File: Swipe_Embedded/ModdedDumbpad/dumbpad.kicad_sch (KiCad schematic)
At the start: 17 parts, among them U1 ESP32-DevKitC

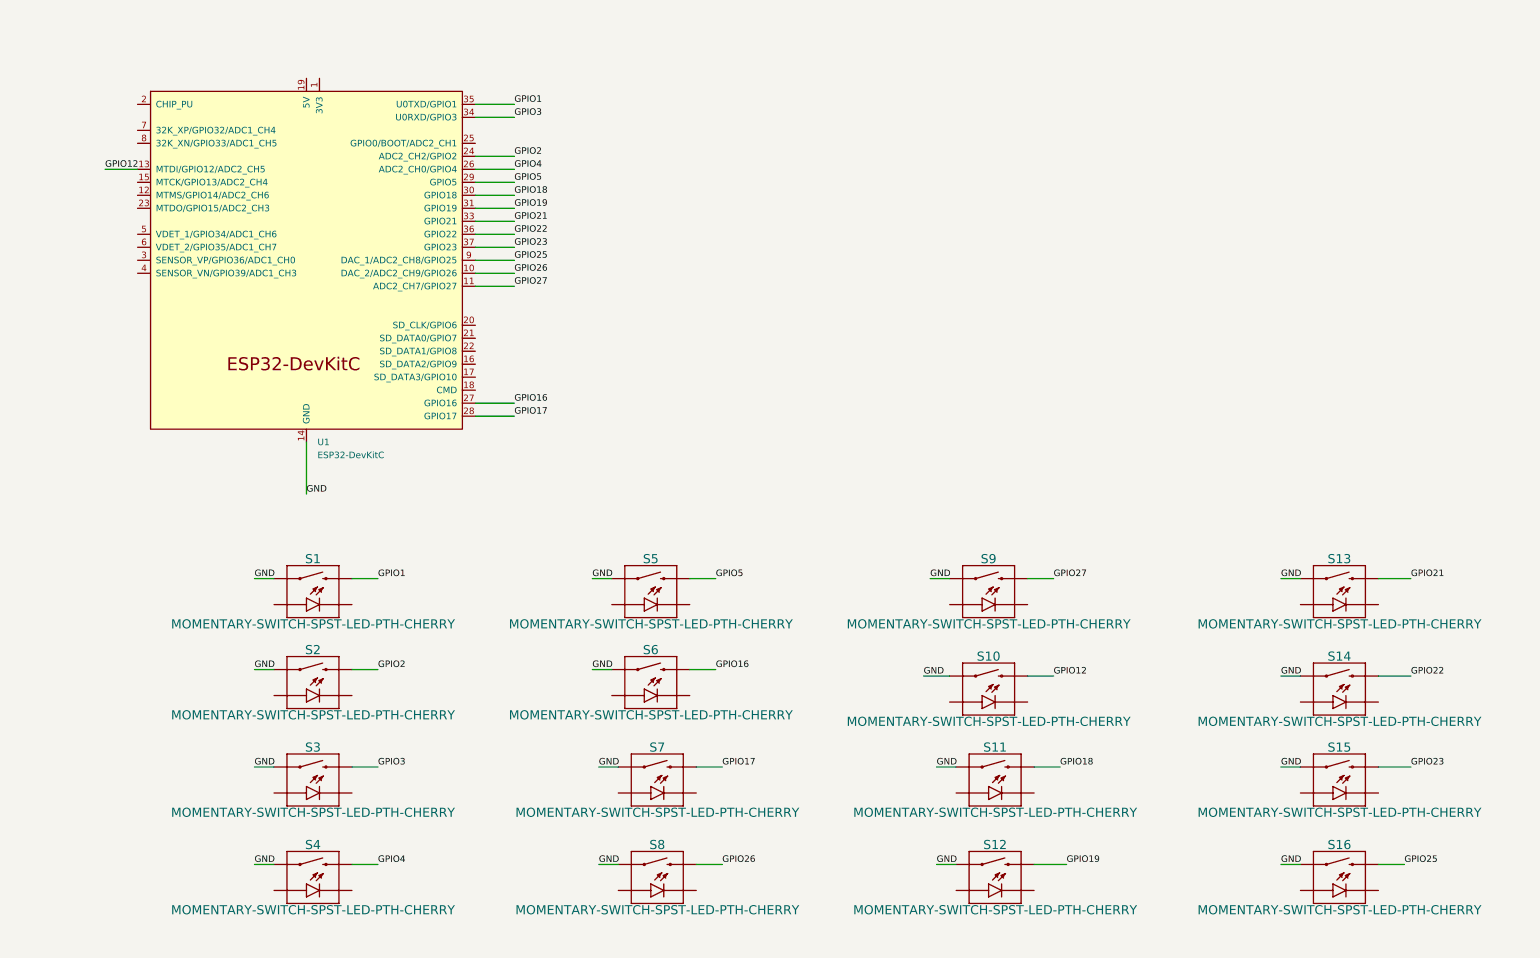
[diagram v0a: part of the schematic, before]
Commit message: *Refactored functions and devices to prepare for swipe pad integration *Improved pcb design
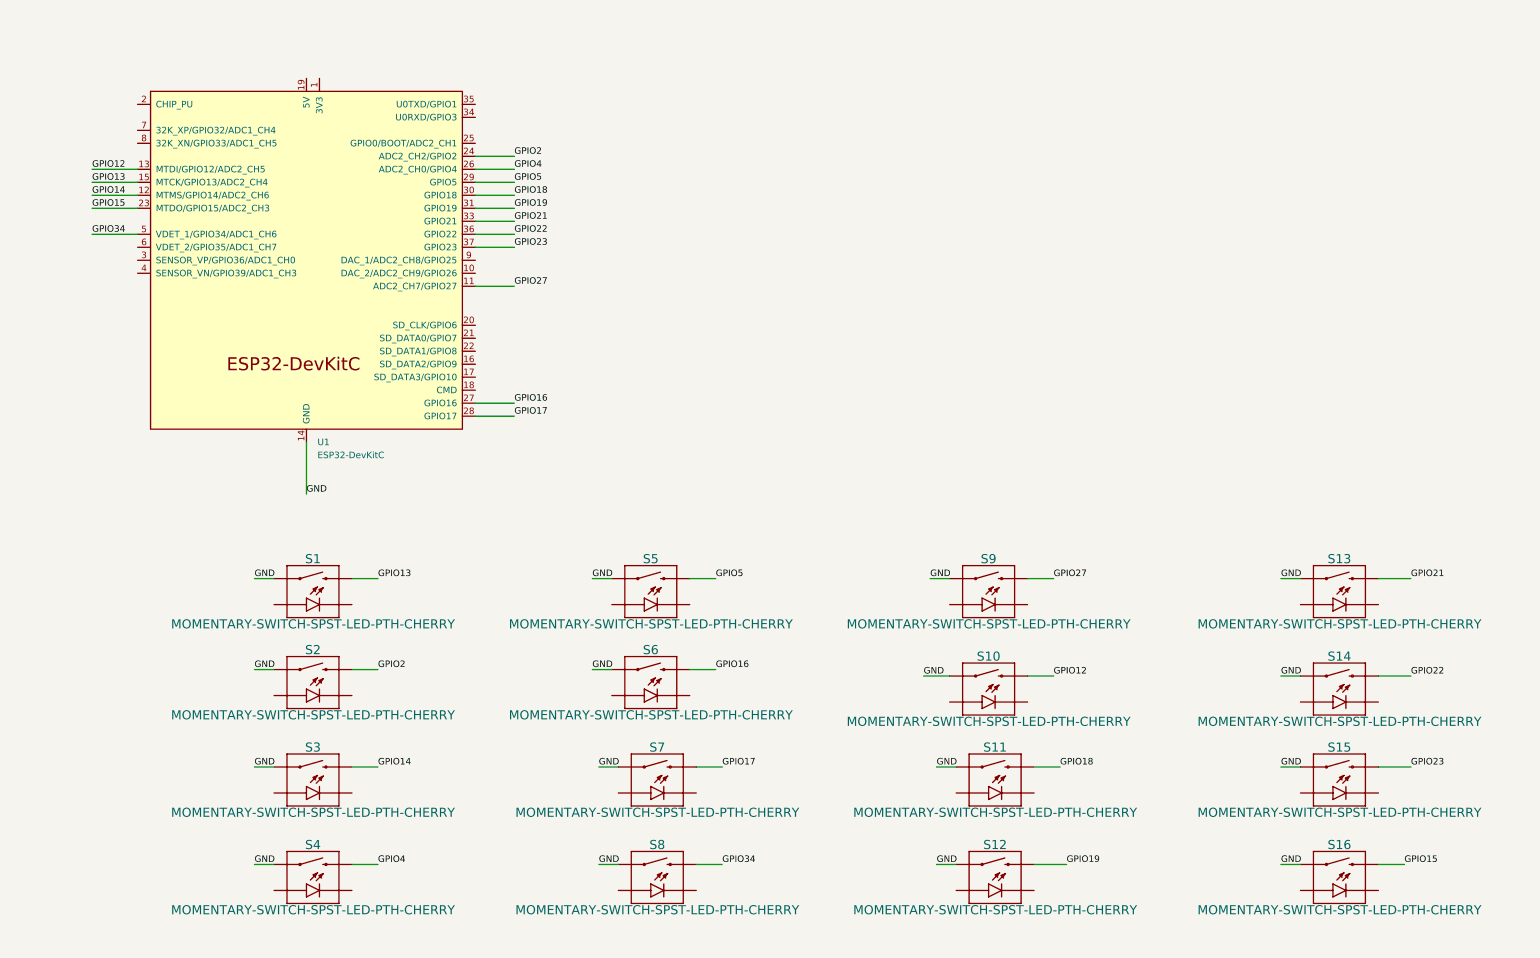
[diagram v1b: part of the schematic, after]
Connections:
- net GPIO14: now reaches U1.12 (MTMS/GPIO14/ADC2_CH6)
- net GPIO14: now also S3.S2 (2)
- net GPIO13: now reaches U1.15 (MTCK/GPIO13/ADC2_CH4)
- net GPIO13: now also S1.S2 (2)
- net GPIO15: now reaches U1.23 (MTDO/GPIO15/ADC2_CH3)
- net GPIO15: now also S16.S2 (2)
- net GPIO34: now reaches U1.5 (VDET_1/GPIO34/ADC1_CH6)
- net GPIO34: now also S8.S2 (2)
- net GPIO1: no longer names the net of U1.35 (U0TXD/GPIO1)
- net GPIO1: no longer S1.S2 (2)
- net GPIO25: no longer names the net of U1.9 (DAC_1/ADC2_CH8/GPIO25)
- net GPIO25: no longer S16.S2 (2)
- net GPIO26: no longer names the net of U1.10 (DAC_2/ADC2_CH9/GPIO26)
- net GPIO26: no longer S8.S2 (2)
- net GPIO3: no longer names the net of U1.34 (U0RXD/GPIO3)
- net GPIO3: no longer S3.S2 (2)
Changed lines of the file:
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@@
 	(wire
 		(pts
-			(xy 120.65 60.96) (xy 128.27 60.96)
+			(xy 45.72 73.66) (xy 54.61 73.66)
+		)
+		(stroke
+			(width 0)
+			(type default)
+		)
+	)
+	(wire
+		(pts
+			(xy 45.72 78.74) (xy 54.61 78.74)
 		)
 		(stroke
@@
 		)
 	)
+	(polyline
+		(pts
+			(xy 330.2 369.57) (xy 358.14 369.57)
+		)
+		(stroke
+			(width 0)
+			(type dash)
+		)
+	)
+	(wire
+		(pts
+			(xy 143.51 168.91) (xy 147.32 168.91)
+		)
+		(stroke
+			(width 0)
+			(type default)
+		)
+	)
+	(wire
+		(pts
+			(xy 96.52 207.01) (xy 101.6 207.01)
+		)
+		(stroke
+			(width 0)
+			(type default)
+		)
+	)
+	(wire
+		(pts
+			(xy 87.63 124.46) (xy 87.63 134.62)
+		)
+		(stroke
+			(width 0)
+			(type default)
+		)
+	)
 	(wire
 		(pts
@@
 	(polyline
 		(pts
-			(xy 330.2 369.57) (xy 358.14 369.57)
-		)
-		(stroke
-			(width 0)
-			(type dash)
-		)
-	)
-	(wire
-		(pts
-			(xy 143.51 168.91) (xy 147.32 168.91)
-		)
-		(stroke
-			(width 0)
-			(type default)
-		)
-	)
-	(wire
-		(pts
-			(xy 96.52 207.01) (xy 101.6 207.01)
-		)
-		(stroke
-			(width 0)
-			(type default)
-		)
-	)
-	(wire
-		(pts
-			(xy 87.63 124.46) (xy 87.63 134.62)
-		)
-		(stroke
-			(width 0)
-			(type default)
-		)
-	)
-	(polyline
-		(pts
 			(xy 358.14 361.95) (xy 330.2 361.95)
 		)
@@
 	(wire
 		(pts
-			(xy 120.65 58.42) (xy 128.27 58.42)
-		)
-		(stroke
-			(width 0)
-			(type default)
-		)
-	)
-	(wire
-		(pts
 			(xy 144.78 207.01) (xy 148.59 207.01)
 		)
@@
 	(wire
 		(pts
-			(xy 48.26 71.12) (xy 54.61 71.12)
+			(xy 45.72 71.12) (xy 54.61 71.12)
 		)
 		(stroke
@@
 	(wire
 		(pts
-			(xy 120.65 91.44) (xy 128.27 91.44)
-		)
-		(stroke
-			(width 0)
-			(type default)
-		)
-	)
-	(wire
-		(pts
-			(xy 120.65 88.9) (xy 128.27 88.9)
-		)
-		(stroke
-			(width 0)
-			(type default)
-		)
-	)
-	(wire
-		(pts
 			(xy 278.13 151.13) (xy 281.94 151.13)
 		)
@@
 	(wire
 		(pts
+			(xy 45.72 76.2) (xy 54.61 76.2)
+		)
+		(stroke
+			(width 0)
+			(type default)
+		)
+	)
+	(wire
+		(pts
 			(xy 77.47 168.91) (xy 81.28 168.91)
 		)
@@
 		(pts
 			(xy 120.65 78.74) (xy 128.27 78.74)
+		)
+		(stroke
+			(width 0)
+			(type default)
+		)
+	)
+	(wire
+		(pts
+			(xy 45.72 83.82) (xy 54.61 83.82)
 		)
 		(stroke
@@
 	)
 	(label "GPIO12"
-		(at 48.26 71.12 0)
+		(at 45.72 71.12 0)
 		(effects
 			(font
@@
 		)
 	)
-	(label "GPIO26"
-		(at 128.27 91.44 0)
+	(label "GPIO34"
+		(at 45.72 83.82 0)
 		(effects
 			(font
@@
 		)
 	)
-	(label "GPIO3"
-		(at 128.27 60.96 0)
+	(label "GPIO14"
+		(at 45.72 76.2 0)
 		(effects
 			(font
@@
 		)
 	)
-	(label "GPIO1"
-		(at 128.27 58.42 0)
+	(label "GPIO13"
+		(at 45.72 73.66 0)
 		(effects
 			(font
@@
 		)
 	)
-	(label "GPIO25"
+	(label "GPIO15"
 		(at 302.26 207.01 0)
 		(effects
@@
 		)
 	)
-	(label "GPIO3"
+	(label "GPIO14"
 		(at 101.6 187.96 0)
 		(effects
@@
 		)
 	)
-	(label "GPIO25"
-		(at 128.27 88.9 0)
+	(label "GPIO15"
+		(at 45.72 78.74 0)
 		(effects
 			(font
@@
 		)
 	)
-	(label "GPIO1"
+	(label "GPIO13"
 		(at 101.6 151.13 0)
 		(effects
@@
 		)
 	)
-	(label "GPIO26"
+	(label "GPIO34"
 		(at 168.91 207.01 0)
 		(effects
